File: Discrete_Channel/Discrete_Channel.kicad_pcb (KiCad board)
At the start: 4 copper layers, 75.4 x 49 mm, 67 parts, among them J1 Conn_01x05_Male, J2 Conn_01x06_Male, J3 Conn_01x05_Male, J4 Banna Jack, U1 TPA3244, U2 LM4562

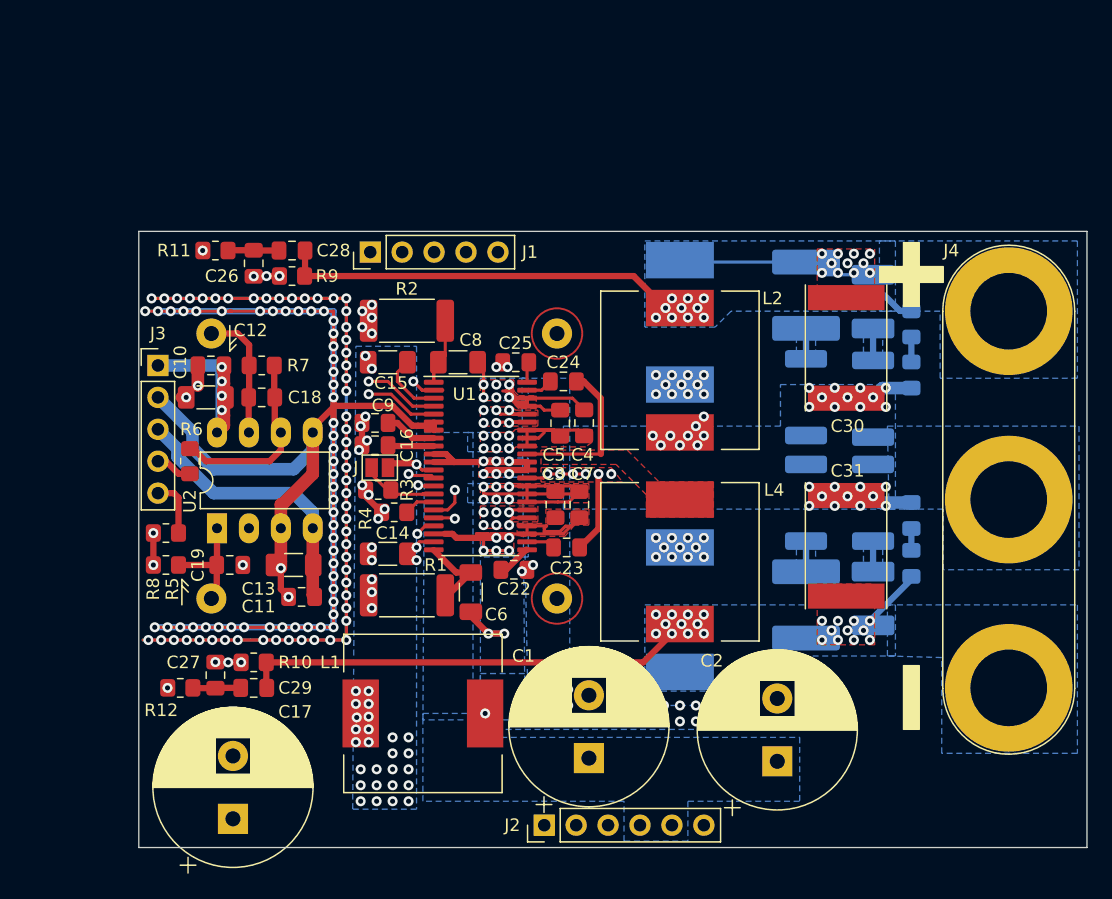
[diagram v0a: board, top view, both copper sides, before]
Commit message: Circuit R2
Fixed Issue with heatsink pad shorting out amplifier.
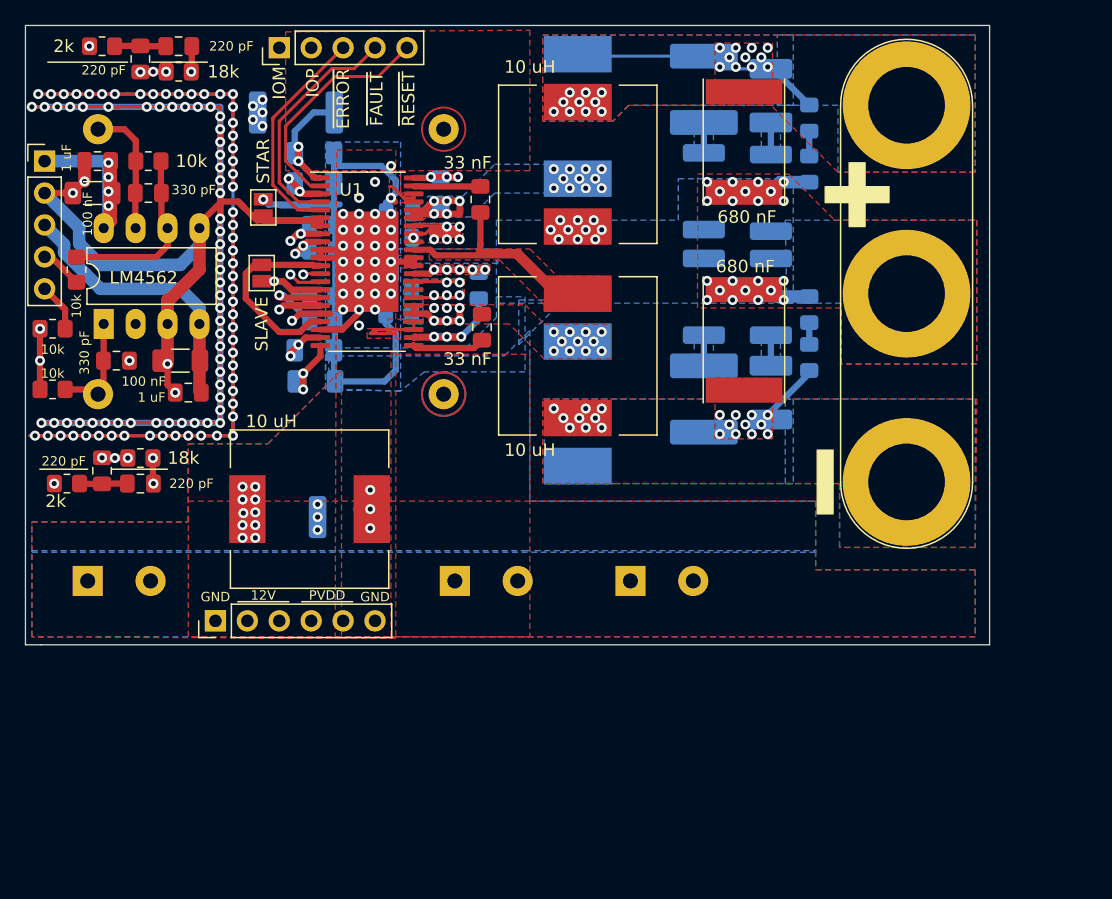
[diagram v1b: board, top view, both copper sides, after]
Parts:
- added STAR: Star_Point, Jumper:SolderJumper-2_P1.3mm_Open_Pad1.0x1.5mm, F.Cu at (132.6, 77.9)
- C1, C14, C15, C16, C17, C2, C23, C25, C3, C4, C5, C6, C7, C8, C9, R1, R2, R3, R4: moved to B.Cu
- moved J2 30.8 mm to (128.8, 110.7)
- moved C7 22.4 mm to (143.4, 84.3), turned to 180 degrees
- moved C17 22.2 mm to (118.6, 107.6), turned to 0 degrees
- moved C23 22.0 mm to (149.7, 84.1), turned to 90 degrees
- moved C5 21.1 mm to (143.4, 78.2), turned to 180 degrees
- moved C4 20.8 mm to (143.4, 80.3), turned to 180 degrees
- moved C6 20.8 mm to (136.7, 91.7), turned to 180 degrees
- moved C8 20.2 mm to (136.7, 73.5)
- moved C3 19.6 mm to (143.4, 86.4), turned to 180 degrees
- moved C22 19.5 mm to (150.0, 87.4), turned to 90 degrees
- moved R2 18.8 mm to (135.2, 70.3)
- moved L1 18.6 mm to (136.3, 101.9)
- moved U1 18.6 mm to (140.8, 82.2)
- moved C13 18.6 mm to (126.0, 90.0)
- moved C18 18.6 mm to (123.4, 76.7)
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- renumbered J to SLAVE
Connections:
- J1 pad 1: /~FAULT -> /OSC_IOM
- J1 pad 2: /~RESET -> /OSC_IOP
- J1 pad 3: /OSC_IOM -> /~RESET
- J1 pad 4: /OSC_IOP -> /~FAULT
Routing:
- net GND: track 86.3 -> 119.8 mm, vias 102 -> 55
- net /PVDD: track 32.3 -> 15.6 mm, vias 12 -> 11
- net /OUT_C: track 13.9 -> 28.1 mm
- net Net-(C6-Pad2): track 6.47 -> 19.1 mm, vias 0 -> 5
- net Net-(C23-Pad1): track 2.29 -> 13.4 mm, vias 0 -> 3
- net /SPEAKER-: track 41.2 -> 51.3 mm
- net GNDA: track 368.5 -> 378.6 mm
- net Net-(C21-Pad1): track 21.6 -> 31.5 mm
- net Net-(C20-Pad1): track 14.8 -> 20.7 mm
- net /DVDD: track 11.8 -> 16.7 mm, vias 2 -> 0
- net /OUT_A: track 25.9 -> 21.4 mm, vias 19 -> 17
- net Net-(C25-Pad1): track 1.65 -> 5.74 mm, vias 0 -> 3
- net Net-(R4-Pad2): track 2.85 -> 6.65 mm, vias 0 -> 1
- net /SPEAKER+: track 53.6 -> 57.0 mm, vias 21 -> 22
- net Net-(C14-Pad2): track 22.4 -> 25.6 mm, vias 3 -> 5
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- added copper zone on In1.Cu, net /+12V
- added copper zone on In2.Cu, net /OUT_A
- added copper zone on In2.Cu, net /OUT_B
- added copper zone on B.Cu, net /OUT_D
- added copper zone on In2.Cu, net /OUT_D
- added copper zone on In1.Cu, net /PVDD
- added copper zone on In1.Cu, net /SPEAKER+
- added copper zone on In2.Cu, net /SPEAKER+
- added copper zone on In1.Cu, net /SPEAKER-
- added copper zone on In2.Cu, net /SPEAKER-
- added copper zone on In2.Cu, net GND
- removed copper zone on In1.Cu, net (none)
- removed copper zone on In2.Cu, net (none)
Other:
- board size 75.4 x 49 mm -> 76.7 x 49.3 mm
- net class Analog_Small_Signal: clearance 0.2 -> 0.1
- net class Digital_Small_Signal: clearance 0.2 -> 0.1
- net class Power: clearance 0.2 -> 0.1
- net class Power_Amp_Out_Thin: clearance 0.2 -> 0.1
- net class Power_Thin: clearance 0.2 -> 0.1
- board text added: "+"
- board text added: "-"
- board text added: "12V"
- board text added: "A"
- board text added: "A+"
- board text added: "A-"
- board text added: "B"
- board text added: "B+"
- board text added: "B-"
- board text added: "FB_A"
- board text added: "FB_B"
- board text added: "G"
- board text added: "GND"
- board text added: "IOM"
- board text added: "IOP"
- board text added: "PVDD"
- board text added: "VCC"
- board text added: "VEE"
- board text added: "~ERROR"
- board text added: "~FAULT"
- board text added: "~RESET"
